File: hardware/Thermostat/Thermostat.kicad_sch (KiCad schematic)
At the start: 50 parts, among them J1 MainConnectorr, J2 Screw_Terminal_01x02, J3 AVR-ISP-6, K1 G6E, K2 G6E, K3 G6E, K4 G6E, SW5_RESET1 SW_Push, U1 GU112X16G-7003BL, U4 UA78M05QDCYRQ1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

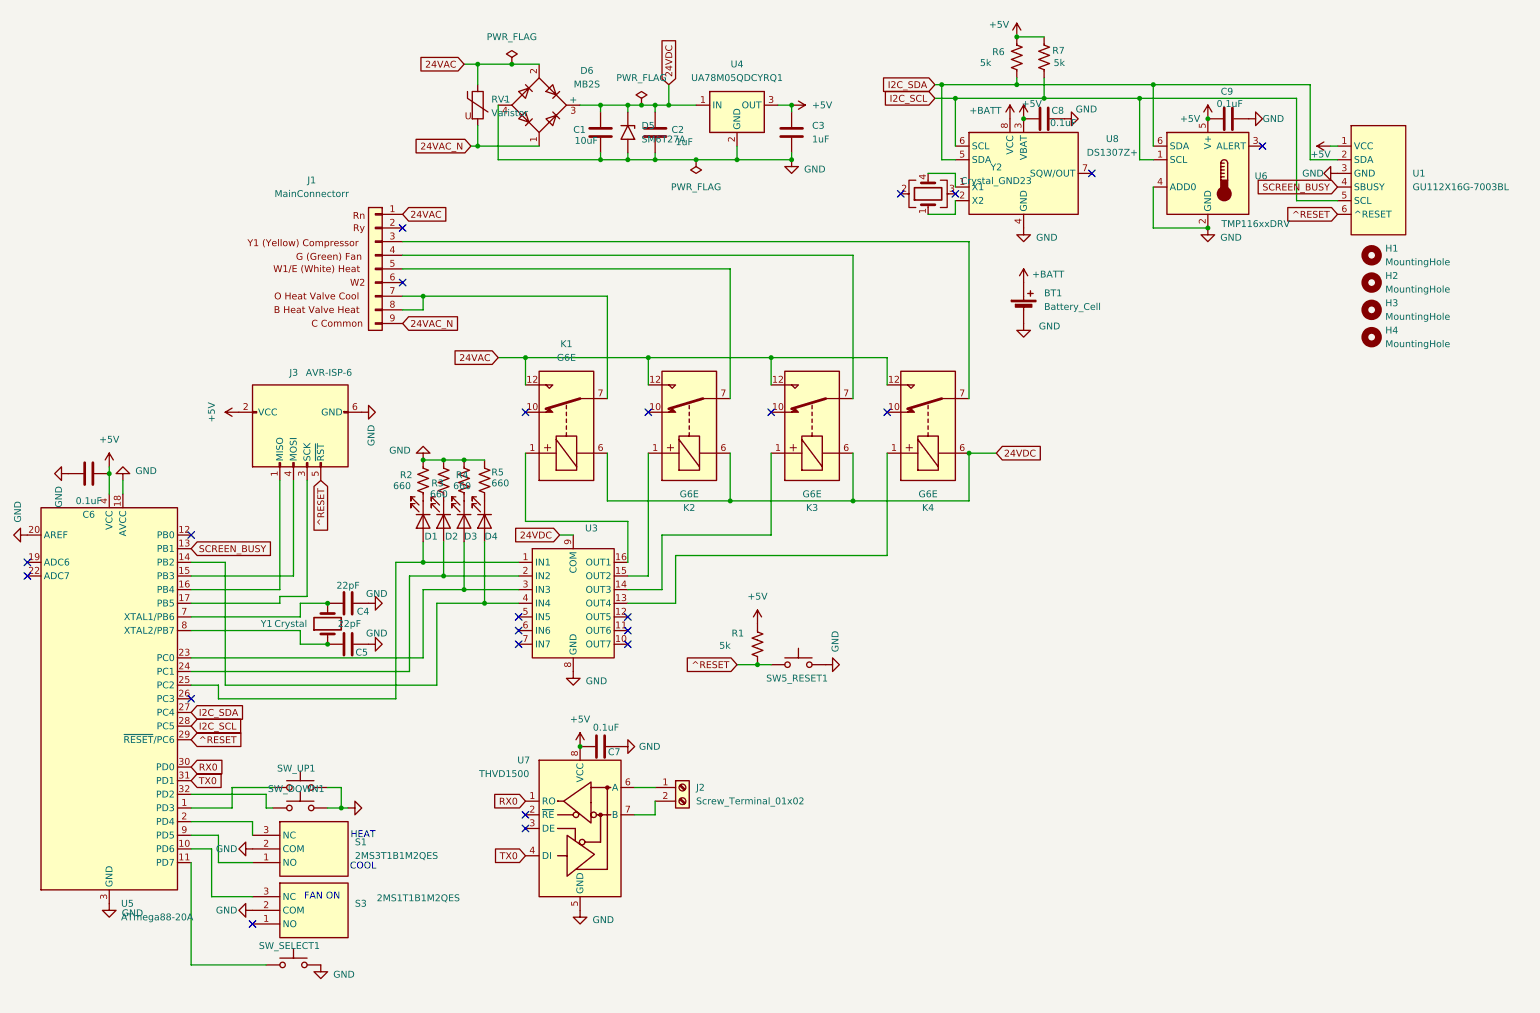
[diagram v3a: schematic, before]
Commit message: Support reverse valve. Change out connector. Put in right parts
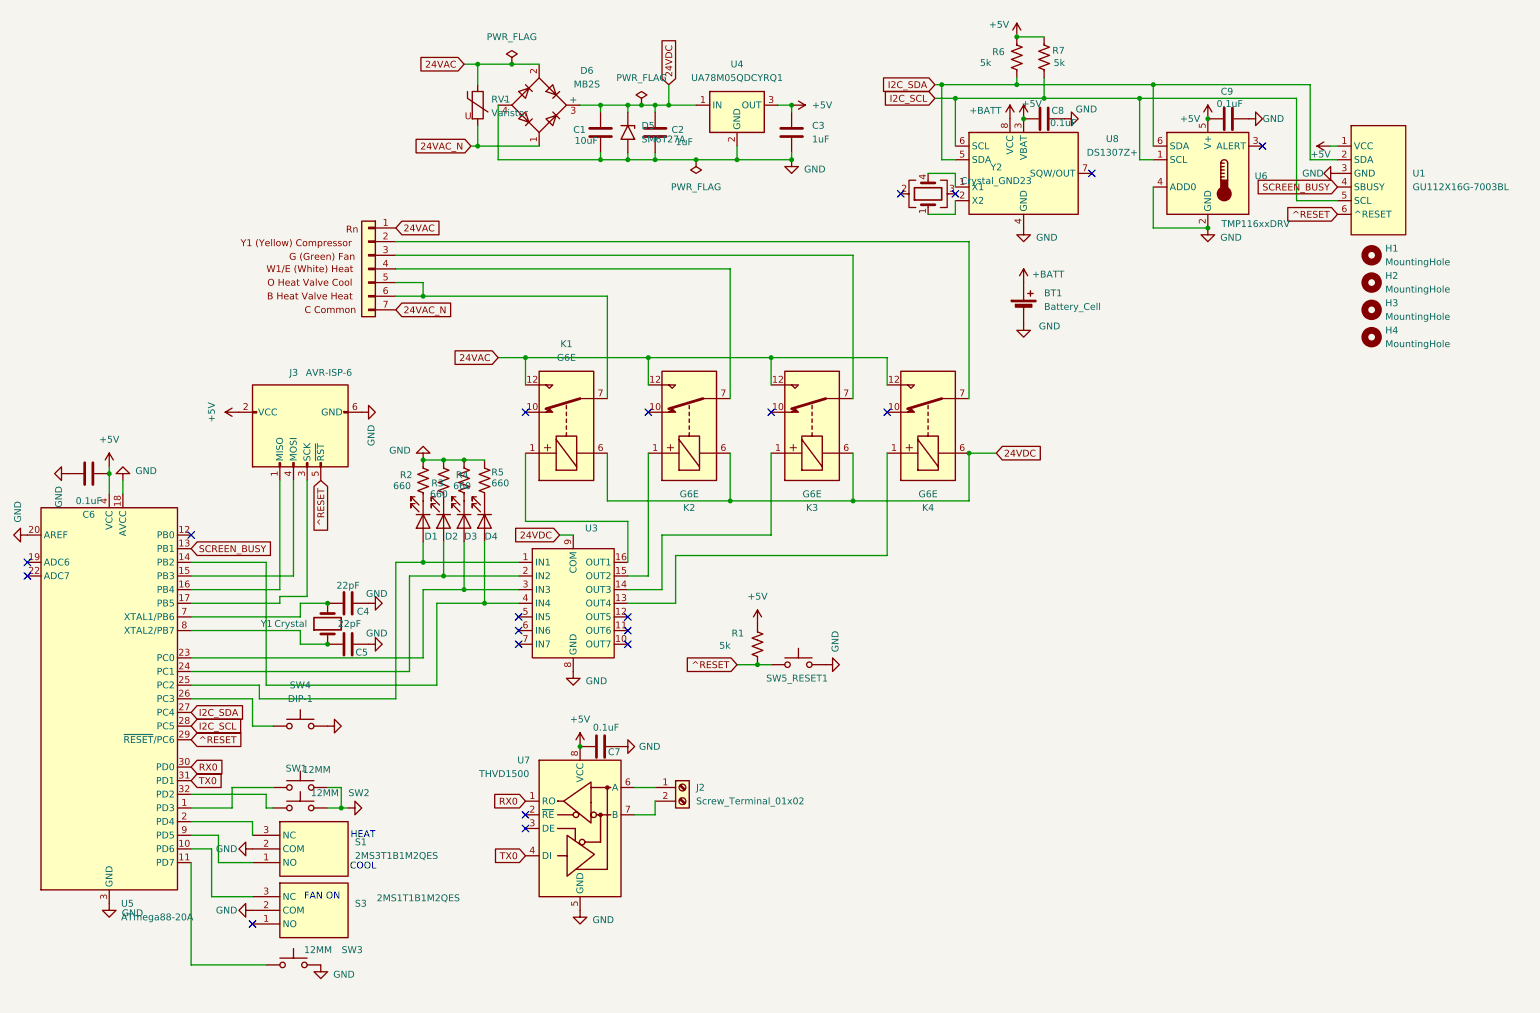
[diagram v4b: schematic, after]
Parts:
- removed J1: MainConnectorr, TerminalBlock_Phoenix:TerminalBlock_Phoenix_MKDS-3-9-5.08_1x09_P5.08mm_Horizontal, symbol ThermoSymbols:MainConnectorr
- removed SW_DOWN1, SW_SELECT1: SW_Push, Button_Switch_THT:SW_PUSH-12mm, symbol Switch:SW_Push
- added J4: MainConnectorr, TerminalBlock:TerminalBlock_MaiXu_MX126-5.0-07P_1x07_P5.00mm, symbol ThermoSymbols:MainConnectorr_1
- added SW2, SW3: 12MM, Button_Switch_THT:SW_PUSH-12mm, symbol Switch:SW_Push
- added SW4: DIP-1, Button_Switch_SMD:SW_DIP_SPSTx01_Slide_6.7x4.1mm_W6.73mm_P2.54mm_LowProfile_JPin, symbol Switch:SW_Push
- SW1: renamed from SW_UP1; value SW_Push -> 12MM
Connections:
- net 24VAC: now also J4.1 (Pin_1)
- net 24VAC_N: now also J4.7 (Pin_7)
- net GND: now also SW2.2, SW3.2, SW4.2
- net at U5.11 (PD7): now also SW3.1
- net at K4.7: now also J4.2 (Pin_2)
- net at K3.7: now also J4.3 (Pin_3)
- net at K2.7: now also J4.4 (Pin_4)
- net at K1.7: now also J4.5 (Pin_5), J4.6 (Pin_6)
- net at U5.26 (PC3): now also SW4.1
- net at U5.32 (PD2): now also SW2.1
- no-connect marks 23 -> 20

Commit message: Sent to fab, whoohoo
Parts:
- added H5, H6, H7, H8: MountingHole, MountingHole:MountingHole_2mm, symbol Mechanical:MountingHole
- S1: value 2MS3T1B1M2QES -> 2MS1T1B1M2QES
- renumbered SW5_RESET1 to SW5
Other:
- note added: "Should be 2MS3T1B1M2QES"

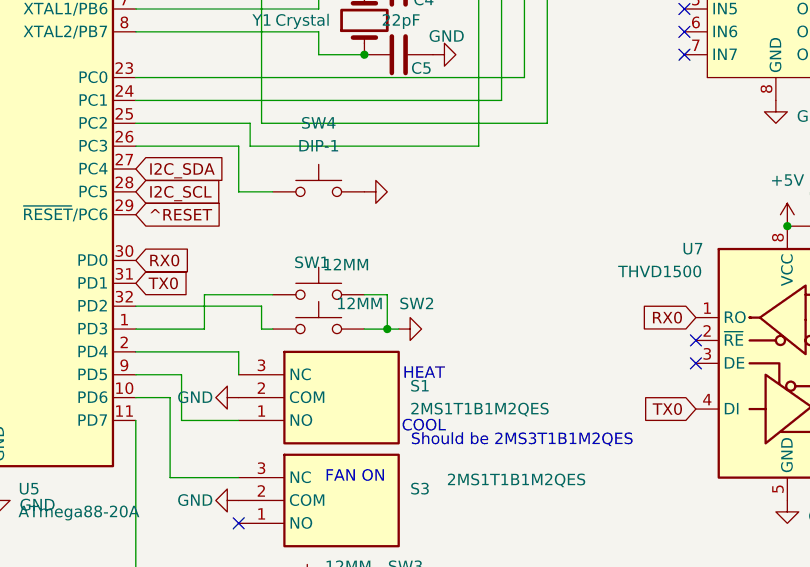
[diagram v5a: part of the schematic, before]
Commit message: Add up/down text on buttons to be clear
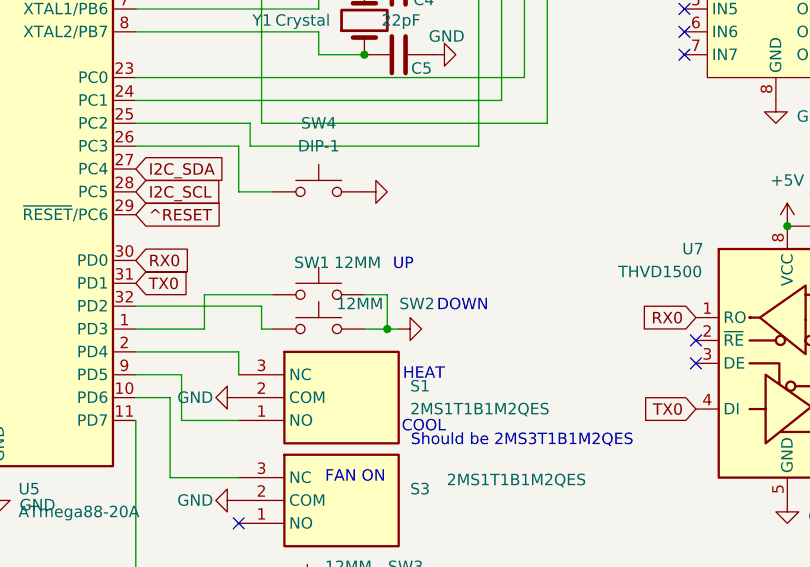
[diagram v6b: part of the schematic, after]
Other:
- note added: "DOWN"
- note added: "UP"
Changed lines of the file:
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@@
 		)
 	)
+	(text "DOWN"
+		(exclude_from_sim no)
+		(at 87.122 158.75 0)
+		(effects
+			(font
+				(size 1.27 1.27)
+			)
+		)
+	)
+	(text "UP"
+		(exclude_from_sim no)
+		(at 80.518 154.178 0)
+		(effects
+			(font
+				(size 1.27 1.27)
+			)
+		)
+	)
 	(junction
 		(at 151.13 104.14)
@@
 		)
 		(property "Value" "12MM"
-			(at 74.168 154.178 0)
+			(at 75.438 153.924 0)
 			(effects
 				(font

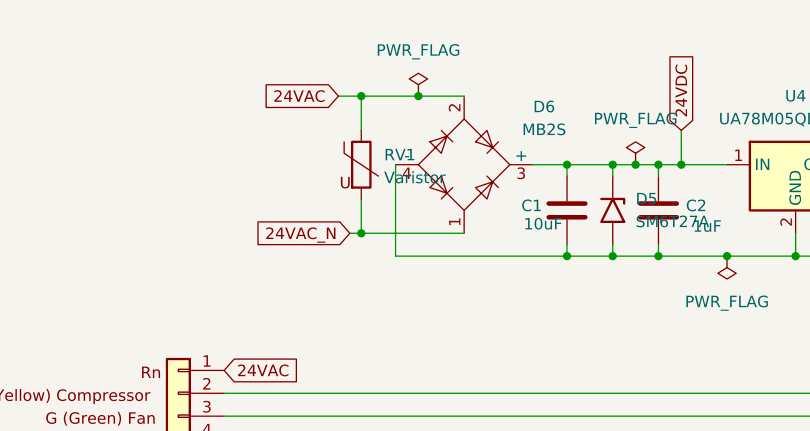
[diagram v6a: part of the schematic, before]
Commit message: Use 24v barrel jack for now. Fix placement issues with screen and buttons
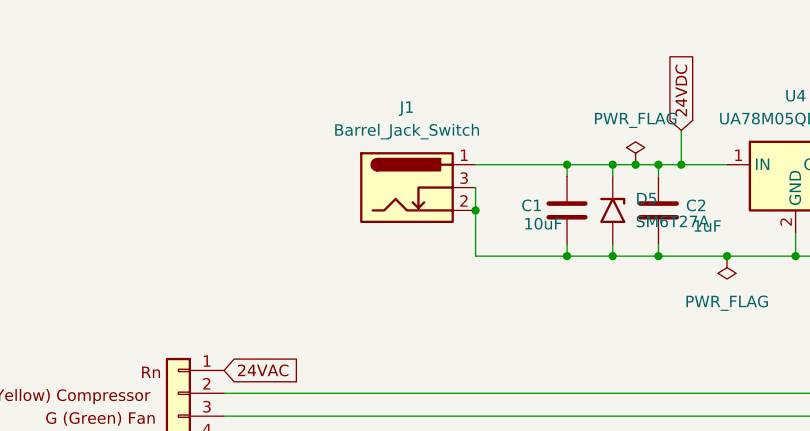
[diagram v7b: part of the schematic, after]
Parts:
- removed D6: MB2S, Package_TO_SOT_SMD:TO-269AA, symbol Diode_Bridge:MB2S
- removed RV1: Varistor, Varistor:RV_Disc_D7mm_W3.7mm_P5mm, symbol Device:Varistor
- added J1: Barrel_Jack_Switch, Connector_BarrelJack:BarrelJack_CUI_PJ-102AH_Horizontal, symbol Connector:Barrel_Jack_Switch
- SW1, SW2, SW3: footprint Button_Switch_THT:SW_PUSH-12mm -> ThermostatFootprints:B3F
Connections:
- net 24VDC: now also J1.1
- net GND: now also J1.2, J1.3

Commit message: Misc fixes for DC power probably
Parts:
- J1: footprint Connector_BarrelJack:BarrelJack_CUI_PJ-102AH_Horizontal -> Connector_BarrelJack:BarrelJack_Wuerth_6941xx301002
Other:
- moved on the sheet: BT1
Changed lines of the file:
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@@
 	)
 	(junction
+		(at 210.82 64.77)
+		(diameter 0)
+		(color 0 0 0 0)
+	)
+	(junction
 		(at 135.89 77.47)
 		(diameter 0)
@@
 	(wire
 		(pts
+			(xy 210.82 63.5) (xy 210.82 64.77)
+		)
+		(stroke
+			(width 0)
+			(type default)
+		)
+	)
+	(wire
+		(pts
 			(xy 50.8 120.65) (xy 67.31 120.65)
 		)
@@
 			)
 		)
-		(property "Footprint" "Connector_BarrelJack:BarrelJack_CUI_PJ-102AH_Horizontal"
+		(property "Footprint" "Connector_BarrelJack:BarrelJack_Wuerth_6941xx301002"
 			(at 110.49 34.036 0)
 			(effects
@@
 	)
 	(symbol
+		(lib_id "power:PWR_FLAG")
+		(at 210.82 64.77 90)
+		(unit 1)
+		(exclude_from_sim no)
+		(in_bom yes)
+		(on_board yes)
+		(dnp no)
+		(fields_autoplaced yes)
+		(property "Reference" "#FLG01"
+			(at 208.915 64.77 0)
+			(effects
+				(font
+					(size 1.27 1.27)
+				)
+				(hide yes)
+			)
+		)
+		(property "Value" "PWR_FLAG"
+			(at 207.01 64.7699 90)
+			(effects
+				(font
+					(size 1.27 1.27)
+				)
+				(justify left)
+			)
+		)
+		(property "Footprint" ""
+			(at 210.82 64.77 0)
+			(effects
+				(font
+					(size 1.27 1.27)
+				)
+				(hide yes)
+			)
+		)
+		(property "Datasheet" "~"
+			(at 210.82 64.77 0)
+			(effects
+				(font
+					(size 1.27 1.27)
+				)
+				(hide yes)
+			)
+		)
+		(property "Description" "Special symbol for telling ERC where power comes from"
+			(at 210.82 64.77 0)
+			(effects
+				(font
+					(size 1.27 1.27)
+				)
+				(hide yes)
+			)
+		)
+		(pin "1"
+		)
+		(instances
+			(project "Thermostat"
+				(path "/dae3c193-ffe6-4911-a810-cfe956c95f3b"
+					(reference "#FLG01")
+					(unit 1)
+				)
+			)
+		)
+	)
+	(symbol
 		(lib_id "Switch:SW_Push")
 		(at 69.85 190.5 0)
@@
 	(symbol
 		(lib_id "power:+BATT")
-		(at 205.74 63.5 0)
+		(at 210.82 63.5 0)
 		(unit 1)
 		(exclude_from_sim no)
@@
 		(dnp no)
 		(property "Reference" "#PWR04"
-			(at 205.74 67.31 0)
+			(at 210.82 67.31 0)
 			(effects
 				(font
@@
 		)
 		(property "Value" "+BATT"
-			(at 210.312 61.976 0)
+			(at 215.392 61.976 0)
 			(effects
 				(font
@@
 		)
 		(property "Footprint" ""
-			(at 205.74 63.5 0)
+			(at 210.82 63.5 0)
 			(effects
 				(font
@@
 		)
 		(property "Datasheet" ""
-			(at 205.74 63.5 0)
+			(at 210.82 63.5 0)
 			(effects
 				(font
@@
 		)
 		(property "Description" "Power symbol creates a global label with name \"+BATT\""
-			(at 205.74 63.5 0)
+			(at 210.82 63.5 0)
 			(effects
 				(font
@@
 	(symbol
 		(lib_id "power:GND")
-		(at 205.74 71.12 0)
+		(at 210.82 72.39 0)
 		(unit 1)
 		(exclude_from_sim no)
@@
 		(dnp no)
 		(property "Reference" "#PWR03"
-			(at 205.74 77.47 0)
+			(at 210.82 78.74 0)
 			(effects
 				(font
@@
 		)
 		(property "Value" "GND"
-			(at 210.566 71.628 0)
+			(at 215.646 72.898 0)
 			(effects
 				(font
@@
 		)
 		(property "Footprint" ""
-			(at 205.74 71.12 0)
+			(at 210.82 72.39 0)
 			(effects
 				(font
@@
 		)
 		(property "Datasheet" ""
-			(at 205.74 71.12 0)
+			(at 210.82 72.39 0)
 			(effects
 				(font
@@
 		)
 		(property "Description" "Power symbol creates a global label with name \"GND\" , ground"
-			(at 205.74 71.12 0)
+			(at 210.82 72.39 0)
 			(effects
 				(font
@@
 	(symbol
 		(lib_id "Device:Battery_Cell")
-		(at 205.74 68.58 0)
+		(at 210.82 69.85 0)
 		(unit 1)
 		(exclude_from_sim no)
@@
 		(fields_autoplaced yes)
 		(property "Reference" "BT1"
-			(at 209.55 65.4684 0)
+			(at 214.63 66.7384 0)
 			(effects
 				(font
@@
 		)
 		(property "Value" "Battery_Cell"
-			(at 209.55 68.0084 0)
+			(at 214.63 69.2784 0)
 			(effects
 				(font
@@
 		)
 		(property "Footprint" "Battery:BatteryHolder_Keystone_1058_1x2032"
-			(at 205.74 67.056 90)
+			(at 210.82 68.326 90)
 			(effects
 				(font
@@
 		)
 		(property "Datasheet" "~"
-			(at 205.74 67.056 90)
+			(at 210.82 68.326 90)
 			(effects
 				(font
@@
 		)
 		(property "Description" "Single-cell battery"
-			(at 205.74 68.58 0)
+			(at 210.82 69.85 0)
 			(effects
 				(font
